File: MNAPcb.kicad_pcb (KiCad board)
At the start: 2 copper layers, 116 parts, among them J2 DA15_Socket, J3 USB_C_Receptacle_USB2.0_16P, J4 Conn_Coaxial, J5 SineWaveIn1, J6 SineWaveIn, J8 Conn_01x05_Pin, SW1 SW_Push_Shielded, U1 STM32F407VGTx, U10 USBLC6-2SC6, U11 INA226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

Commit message: New PCB Changes
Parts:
- added D12: Diode, Diode_SMD:D_0805_2012Metric_Pad1.15x1.40mm_HandSolder, F.Cu at (182.2, 37.4)
- added D13: Diode, Diode_SMD:D_0805_2012Metric_Pad1.15x1.40mm_HandSolder, F.Cu at (182.2, 40.5)
- added D14: Diode, Diode_SMD:D_0805_2012Metric_Pad1.15x1.40mm_HandSolder, F.Cu at (182.2, 43.5)
- added D15: Diode, Diode_SMD:D_0805_2012Metric_Pad1.15x1.40mm_HandSolder, F.Cu at (182.2, 46.5)
- added J7: Conn_01x02, Connector_TE-Connectivity:TE_826576-2_1x02_P3.96mm_Vertical, F.Cu at (145.0, 62.0)
- added PS1: LMS78_15-1.0R, Library:CONV_LMS78_15-1.0R, F.Cu at (271.0, 91.8)
- added PS2: LMS78_15-1.0R, Library:CONV_LMS78_15-1.0R, F.Cu at (271.0, 106.3)
- added R35: 470, Resistor_SMD:R_0805_2012Metric, F.Cu at (182.0, 49.5)
- added R36: 470, Resistor_SMD:R_0805_2012Metric, F.Cu at (182.0, 52.5)
- added R37: 470, Resistor_SMD:R_0805_2012Metric, F.Cu at (182.0, 55.4)
- added R38: 470, Resistor_SMD:R_0805_2012Metric, F.Cu at (182.0, 58.4)
- added U14: TIP29A, Library:TO-220AB_ONS, F.Cu at (159.4, 25.5)
- added U15: TIP29A, Library:TO-220AB_ONS, F.Cu at (244.4, 31.5)
- added U16: TIP29A, Library:TO-220AB_ONS, F.Cu at (230.9, 38.5)
- added U17: TIP29A, Library:TO-220AB_ONS, F.Cu at (229.4, 25.5)
- added U19: TPS54202DDCR, Library:SOT95P280X110-6N, F.Cu at (265.6, 121.5)
- added U5: TPS54202DDCR, Library:SOT95P280X110-6N, F.Cu at (257.9, 114.5)
- added U8: TPS54202DDCR, Library:SOT95P280X110-6N, F.Cu at (259.7, 109.0)
- moved C9 133.7 mm to (49.0, 168.0), turned to 90 degrees
- moved C10 131.8 mm to (52.0, 172.4), turned to -90 degrees
- moved C8 129.0 mm to (52.0, 168.0), turned to 90 degrees
- moved FB1 128.1 mm to (49.0, 172.0), turned to 180 degrees
- moved C13 123.1 mm to (47.0, 153.0), turned to 90 degrees
- moved C12 121.4 mm to (50.1, 153.0)
- moved Y1 120.0 mm to (43.0, 156.0), turned to 180 degrees
- moved R2 116.9 mm to (55.0, 151.0)
- moved C11 114.1 mm to (51.0, 164.0), turned to 180 degrees
- moved C15 109.0 mm to (66.0, 174.0)
- moved R1 106.9 mm to (60.0, 151.0)
- moved U1 104.6 mm to (62.0, 164.0)
- moved C14 102.7 mm to (73.1, 160.0)
- moved C1 96.7 mm to (72.0, 157.0), turned to -90 degrees
- moved C7 95.6 mm to (90.0, 156.4), turned to -90 degrees
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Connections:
- J2 pad 13: unconnected-(J2-P13-Pad13) -> /RelayControl/K4OUT
- J2 pad 14: unconnected-(J2-P14-Pad14) -> /RelayControl/K3OUT
- J2 pad 15: unconnected-(J2-P15-Pad15) -> /RelayControl/K2OUT
- J2 pad 6: unconnected-(J2-Pad6) -> /RelayControl/K1OUT
- J3 pad A7: GND -> /UART/D-
- J3 pad B7: GND -> /UART/D-
- U1 pad 41: unconnected-(U1-PE10-Pad41) -> /L298/IN4
- U1 pad 42: /L298/IN4 -> /MCU/K1IN
- U1 pad 43: unconnected-(U1-PE12-Pad43) -> /MCU/K2IN
- U1 pad 44: unconnected-(U1-PE13-Pad44) -> /MCU/K3IN
- U1 pad 45: unconnected-(U1-PE14-Pad45) -> /MCU/K4IN
- U10 pad 4: GND -> /UART/D-

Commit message: FInal Changes in Schgematic
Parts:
- added H1: MountingHole, MountingHole:MountingHole_3.2mm_M3_DIN965, F.Cu at (162.0, 33.0)
- added H2: MountingHole, MountingHole:MountingHole_3.2mm_M3_DIN965, F.Cu at (101.0, 33.0)
- added H3: MountingHole, MountingHole:MountingHole_3.2mm_M3_DIN965, F.Cu at (168.0, 97.0)
- added H4: MountingHole, MountingHole:MountingHole_3.2mm_M3_DIN965, F.Cu at (100.0, 99.0)
- added J1: Conn_01x03_Pin, Connector_Molex:Molex_KK-254_AE-6410-03A_1x03_P2.54mm_Vertical, F.Cu at (130.0, 69.8)
- added J9: Conn_01x02, Connector_TE-Connectivity:TE_826576-2_1x02_P3.96mm_Vertical, F.Cu at (139.8, 60.6)
- added R39: 50m, Resistor_SMD:R_2512_6332Metric_Pad1.40x3.35mm_HandSolder, F.Cu at (113.8, 68.7)
- added R40: 50m, Resistor_SMD:R_2512_6332Metric_Pad1.40x3.35mm_HandSolder, F.Cu at (113.8, 73.6)
- added R41: 50m, Resistor_SMD:R_2512_6332Metric_Pad1.40x3.35mm_HandSolder, F.Cu at (113.8, 78.5)
- added R6: 50m, Resistor_SMD:R_2512_6332Metric_Pad1.40x3.35mm_HandSolder, F.Cu at (113.8, 58.9)
- added R8: 50m, Resistor_SMD:R_2512_6332Metric_Pad1.40x3.35mm_HandSolder, F.Cu at (113.8, 63.8)
- added U18: INA226, Package_SO:VSSOP-10_3x3mm_P0.5mm, F.Cu at (122.0, 63.3)
- added U20: INA226, Package_SO:VSSOP-10_3x3mm_P0.5mm, F.Cu at (122.0, 67.8)
- added U21: INA226, Package_SO:VSSOP-10_3x3mm_P0.5mm, F.Cu at (122.0, 72.4)
- added U22: INA226, Package_SO:VSSOP-10_3x3mm_P0.5mm, F.Cu at (122.0, 77.0)
- added U4: INA226, Package_SO:VSSOP-10_3x3mm_P0.5mm, F.Cu at (122.0, 58.7)
- J5: value SineWaveIn1 -> Conn_01x02; footprint Connector_Coaxial:SMA_Amphenol_132289_EdgeMount -> Connector_TE-Connectivity:TE_826576-2_1x02_P3.96mm_Vertical
- moved U15 193.0 mm to (89.0, 146.0), turned to 90 degrees
- moved J2 184.6 mm to (38.6, 177.7), turned to -90 degrees
- moved U16 176.8 mm to (97.0, 154.0), turned to 90 degrees
- moved U17 172.8 mm to (97.4, 137.0), turned to 90 degrees
- moved D10 167.1 mm to (19.0, 37.0), turned to -90 degrees
- moved U10 166.1 mm to (25.9, 33.0)
- moved C2 165.5 mm to (20.0, 31.1)
- moved C16 160.6 mm to (30.0, 29.1), turned to 180 degrees
- moved C20 159.9 mm to (31.0, 32.1), turned to -90 degrees
- moved C19 159.4 mm to (29.4, 36.1)
- moved C23 154.7 mm to (33.4, 95.8), turned to -90 degrees
- moved D9 154.6 mm to (30.0, 40.0), turned to -90 degrees
- moved D11 151.1 mm to (45.0, 30.1)
- moved R12 150.6 mm to (23.0, 40.1), turned to -90 degrees
- moved FB2 150.4 mm to (22.0, 36.1)
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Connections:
- C1 pad 1: +3.3V -> +3.3
- C10 pad 1: +3.3V -> +3.3
- C24 pad 1: +15V -> +15
- C47 pad 1: +3.3V -> +3.3
- C48 pad 1: +3.3V -> +3.3
- C49 pad 1: +3.3V -> +3.3
- C50 pad 1: +3.3V -> +3.3
- C51 pad 1: +3.3V -> +3.3
- C7 pad 1: +3.3V -> +3.3
- D1 pad 1: +15V -> +15
- D1 pad 2: /L298/OUT1 -> /L298/MOTOR1+
- D12 pad 2: +24V -> +24
- D13 pad 2: +24V -> +24
- D14 pad 2: +24V -> +24
- D15 pad 2: +24V -> +24
- D2 pad 1: /L298/OUT1 -> /L298/MOTOR1+
- D3 pad 1: /L298/OUT2 -> /L298/MOTOR1-
- D4 pad 1: /L298/OUT3 -> /L298/MOTOR2+
- D5 pad 1: /L298/OUT4 -> /L298/MOTOR2-
- D6 pad 1: +15V -> +15
- D6 pad 2: /L298/OUT2 -> /L298/MOTOR1-
- D7 pad 1: +15V -> +15
- D7 pad 2: /L298/OUT3 -> /L298/MOTOR2+
- D8 pad 1: +15V -> +15
- D8 pad 2: /L298/OUT4 -> /L298/MOTOR2-
- FB1 pad 1: +3.3V -> +3.3
- J5 pad 1: /ADC/SineWaveIn -> GND
- J5 pad 2: GND -> +12
- J8 pad 5: +3.3V -> unconnected-(J8-Pin_5-Pad5)
- R1 pad 1: +3.3V -> +3.3
- R2 pad 1: +3.3V -> +3.3
- R4 pad 2: +3.3V -> +3.3
- U1 pad 100: +3.3V -> +3.3
- U1 pad 11: +3.3V -> +3.3
- U1 pad 19: +3.3V -> +3.3
- U1 pad 28: +3.3V -> +3.3
- U1 pad 50: +3.3V -> +3.3
- U1 pad 6: +3.3V -> +3.3
- U1 pad 75: +3.3V -> +3.3
- U11 pad 6: +3.3V -> +3.3
- U12 pad 6: +3.3V -> +3.3
- U13 pad 13: +15V -> +15
- U13 pad 5: +15V -> +15
- U14 pad 2: +24V -> +24
- U15 pad 2: +24V -> +24
- U16 pad 2: +24V -> +24
- U17 pad 3: +24V -> +24
- U2 pad 13: /L298/OUT3 -> /L298/MOTOR2+
- U2 pad 14: /L298/OUT4 -> /L298/MOTOR2-
- U2 pad 2: /L298/OUT1 -> /L298/MOTOR1+
- U2 pad 3: /L298/OUT2 -> /L298/MOTOR1-
- U2 pad 4: +15V -> +15
- U2 pad 9: +5V -> +5

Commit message: Made Changes to Layout and USB C
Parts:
- removed R5, R9: 50m, Resistor_SMD:R_2512_6332Metric_Pad1.40x3.35mm_HandSolder
- removed the R6 at (49.0, 135.0)
- removed the R8 at (56.0, 146.0)
- removed U3, U6, U7: INA226, Package_SO:VSSOP-10_3x3mm_P0.5mm
- removed the U4 at (48.0, 153.0)
- J3: footprint Connector_USB:USB_C_Receptacle_HRO_TYPE-C-31-M-12 -> Connector_USB:USB_C_Receptacle_GCT_USB4085
- J8: footprint Connector_PinHeader_2.54mm:PinHeader_1x05_P2.54mm_Vertical_SMD_Pin1Left -> Connector_PinHeader_2.54mm:PinHeader_1x05_P2.54mm_Vertical
- U2: footprint Package_TO_SOT_THT:TO-220-15_P2.54x2.54mm_StaggerOdd_Lead5.84mm_TabDown -> Package_TO_SOT_THT:TO-220-15_P2.54x5.08mm_StaggerEven_Lead4.58mm_Vertical
- moved C44 135.3 mm to (144.5, 131.0), turned to 90 degrees
- moved C43 133.0 mm to (147.5, 121.0), turned to -90 degrees
- moved C45 128.2 mm to (149.5, 131.0), turned to 90 degrees
- moved U8 127.5 mm to (150.5, 118.0), turned to 90 degrees
- moved C42 126.7 mm to (151.5, 124.0), turned to 180 degrees
- moved C41 126.1 mm to (151.5, 127.0), turned to 180 degrees
- moved J8 124.8 mm to (188.1, 67.5), turned to -90 degrees
- moved R32 122.6 mm to (153.5, 131.0), turned to 90 degrees
- moved C46 122.3 mm to (155.5, 120.0), turned to 90 degrees
- moved C22 120.3 mm to (172.5, 79.0)
- moved L4 119.3 mm to (156.5, 126.0), turned to -90 degrees
- moved R33 118.4 mm to (156.5, 131.0), turned to 90 degrees
- moved R34 114.1 mm to (159.5, 131.0), turned to 90 degrees
- moved C1 113.7 mm to (158.9, 50.1)
- moved C10 113.7 mm to (170.9, 75.1)
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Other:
- board outline added: 115 x 102.5 mm

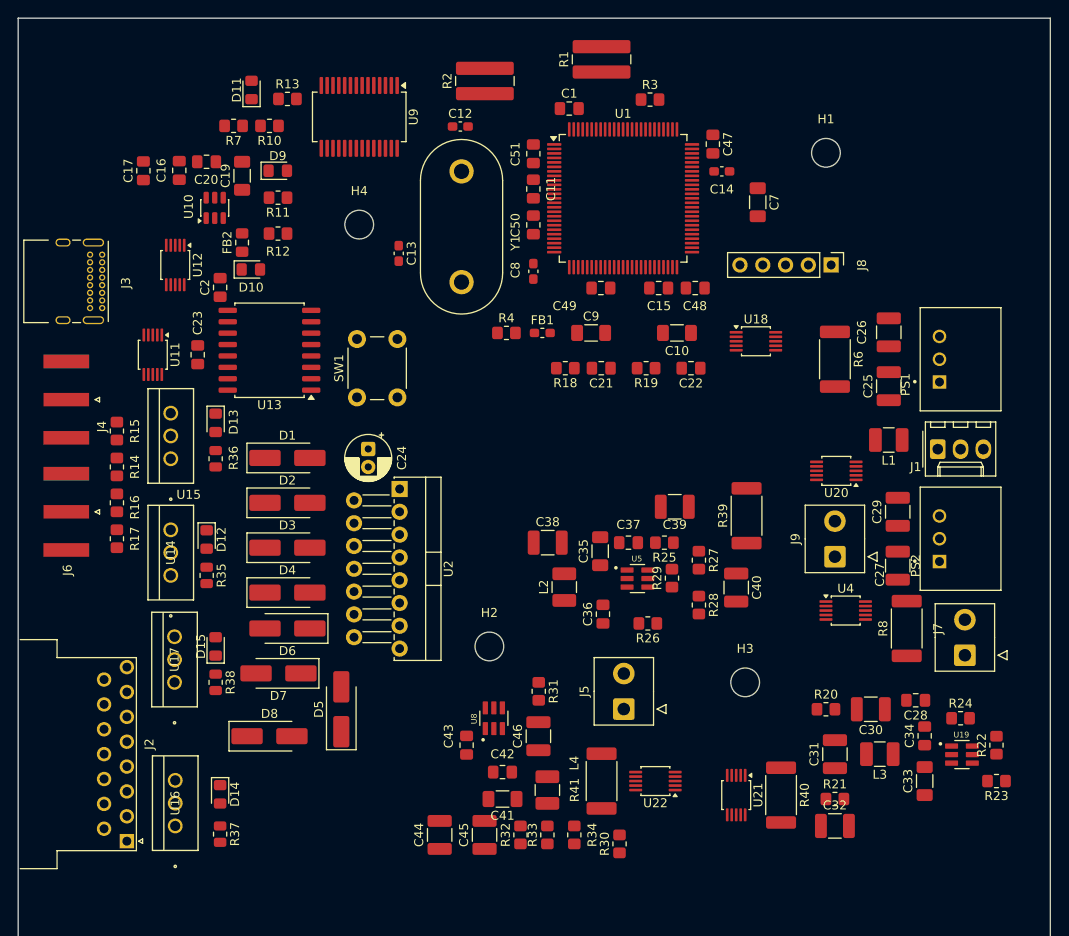
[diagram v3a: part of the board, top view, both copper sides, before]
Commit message: Fixed the Silkscreen issue
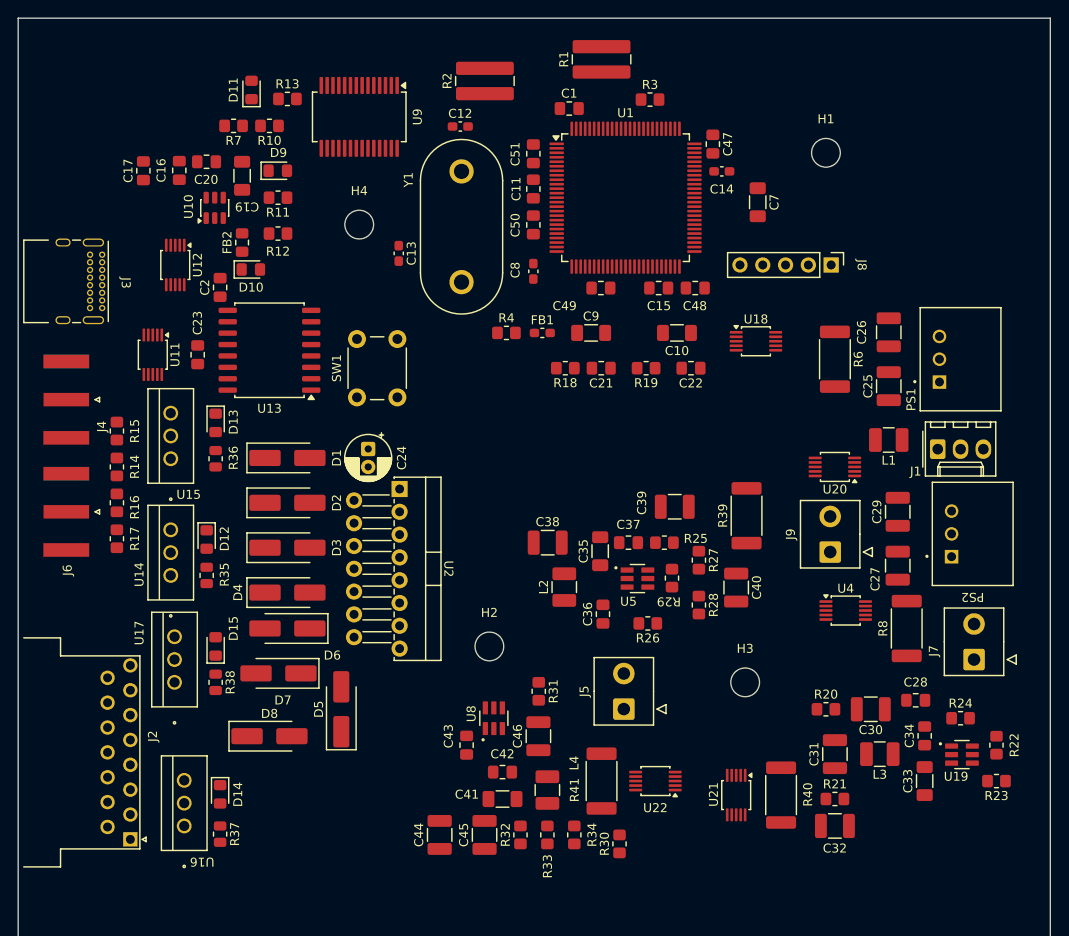
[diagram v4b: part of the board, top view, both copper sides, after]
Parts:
- moved PS2 1.45 mm to (203.8, 97.5)
- moved J7 1.13 mm to (204.0, 111.5)
- moved U16 1.00 mm to (116.0, 130.0)
- moved J9 0.74 mm to (188.0, 99.5)
- moved U20 0.46 mm to (188.5, 90.0)
- moved J2 0.44 mm to (110.0, 131.5)
- moved U1 0.28 mm to (165.2, 60.0)

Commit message: Deleted Uneeded Portion
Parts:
- removed C23: 1u, Capacitor_SMD:C_0805_2012Metric_Pad1.18x1.45mm_HandSolder
- removed J4: Conn_Coaxial, Connector_Coaxial:SMA_Amphenol_132289_EdgeMount
- removed J6: SineWaveIn, Connector_Coaxial:SMA_Amphenol_132289_EdgeMount
- removed U13: AD637xRZ, Package_SO:SOIC-16W_7.5x10.3mm_P1.27mm
- J3: footprint Connector_USB:USB_C_Receptacle_GCT_USB4085 -> Connector_USB:USB_C_Receptacle_G-Switch_GT-USB-7010ASV
- J8: value Conn_01x05_Pin -> Conn_01x04_Pin; footprint Connector_PinHeader_2.54mm:PinHeader_1x05_P2.54mm_Vertical -> Connector_JST:JST_EH_B4B-EH-A_1x04_P2.50mm_Vertical
- moved R23 139.8 mm to (70.2, 93.9), turned to -90 degrees
- moved J7 135.7 mm to (75.1, 153.8), turned to 180 degrees
- moved R24 135.3 mm to (70.2, 89.6), turned to -90 degrees
- moved U19 131.8 mm to (73.3, 97.1), turned to 90 degrees
- moved C28 129.5 mm to (69.1, 99.2), turned to -90 degrees
- moved J9 129.0 mm to (67.7, 146.3)
- moved C33 127.1 mm to (73.1, 104.2), turned to -90 degrees
- moved R8 126.8 mm to (75.1, 144.4)
- moved R22 126.6 mm to (81.4, 101.4), turned to -90 degrees
- moved L3 124.1 mm to (70.2, 108.4), turned to 0 degrees
- moved C34 123.4 mm to (76.1, 104.2), turned to -90 degrees
- moved D5 120.9 mm to (41.8, 38.2), turned to 0 degrees
- moved C30 117.5 mm to (75.2, 109.3), turned to 90 degrees
- moved L1 117.1 mm to (77.6, 80.2), turned to 0 degrees
- moved C32 115.8 mm to (77.5, 97.0), turned to -90 degrees
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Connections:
- C25 pad 1: +24V -> +24
- C33 pad 1: +24V -> +24
- C34 pad 1: +24V -> +24
- C35 pad 1: +24V -> +24
- C36 pad 1: +24V -> +24
- C41 pad 1: +24V -> +24
- C42 pad 1: +24V -> +24
- D13 pad 1: /RelayControl/K2OUT -> /ADC/POT2_V
- J2 pad 12: /ADC/POT2_V -> unconnected-(J2-P12-Pad12)
- J2 pad 15: /RelayControl/K2OUT -> /ADC/POT2_V
- J2 pad 4: +12V -> unconnected-(J2-Pad4)
- J2 pad 5: /ADC/POT1_V -> unconnected-(J2-Pad5)
- J2 pad 7: unconnected-(J2-Pad7) -> /ADC/POT1_V
- J2 pad 8: unconnected-(J2-Pad8) -> +12
- J8 pad 1: GND -> /MCU/NRST
- J8 pad 2: /MCU/SWDIO -> /MCU/SWCLK
- J8 pad 3: /MCU/SWCLK -> /MCU/SWDIO
- J8 pad 4: /MCU/NRST -> GND
- L1 pad 1: +24V -> +24
- PS1 pad 1: +24V -> +24
- R23 pad 2: +24V -> +24
- R26 pad 2: +24V -> +24
- R31 pad 2: +24V -> +24
- U1 pad 26: /ADC/ADC2 -> unconnected-(U1-PA3-Pad26)
- U1 pad 29: /MCU/SINE_WAVE -> unconnected-(U1-PA4-Pad29)
- U1 pad 38: /L298/IN1 -> /L298/IN4
- U1 pad 39: /L298/IN2 -> /L298/IN3
- U1 pad 40: /L298/IN3 -> /L298/PWM1
- U1 pad 41: /L298/IN4 -> /L298/IN2
- U1 pad 42: /MCU/K1IN -> /L298/IN1
- U1 pad 43: /MCU/K2IN -> /MCU/K1IN
- U1 pad 44: /MCU/K3IN -> /MCU/K2IN
- U1 pad 45: /MCU/K4IN -> /MCU/K3IN
- U1 pad 46: unconnected-(U1-PE15-Pad46) -> /MCU/K4IN
- U1 pad 47: unconnected-(U1-PB10-Pad47) -> /ADC/SCL_ADC
- U1 pad 48: unconnected-(U1-PB11-Pad48) -> /ADC/SDA_ADC
- U1 pad 67: /L298/PWM1 -> unconnected-(U1-PA8-Pad67)
- U1 pad 92: /ADC/SCL_ADC -> unconnected-(U1-PB6-Pad92)
- U1 pad 93: /ADC/SDA_ADC -> unconnected-(U1-PB7-Pad93)
- U15 pad 3: /RelayControl/K2OUT -> /ADC/POT2_V
- U19 pad 3: +24V -> +24
- U5 pad 3: +24V -> +24
- U8 pad 3: +24V -> +24
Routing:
- net +24: track 0.00 -> 381.2 mm
- net GND: track 0.00 -> 143.4 mm
- net /ADC/SDA_ADC: track 0.00 -> 108.5 mm
- net /ADC/SCL_ADC: track 0.00 -> 104.3 mm
- net +12V: track 0.00 -> 62.7 mm
- net /MCU/NRST: track 0.00 -> 54.6 mm
- net +5V: track 0.00 -> 52.5 mm
- net +3.3: track 0.00 -> 49.3 mm
- net +3.3V: track 0.00 -> 46.9 mm
- net /UART/VCCIO: track 0.00 -> 35.3 mm
- net /UART/USB_VBUS: track 0.00 -> 30.9 mm
- net /ADC/POT2_V: track 0.00 -> 29.3 mm
- net Net-(D10-K): track 0.00 -> 25.8 mm
- net Net-(D11-K): track 0.00 -> 25.1 mm
- net Net-(U1-PH1): track 0.00 -> 23.6 mm
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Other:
- board size 115 x 102.5 mm -> 113.4 x 103.3 mm
